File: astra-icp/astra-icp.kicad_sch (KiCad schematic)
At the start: 45 parts, among them J1 Conn_02x05_Top_Bottom

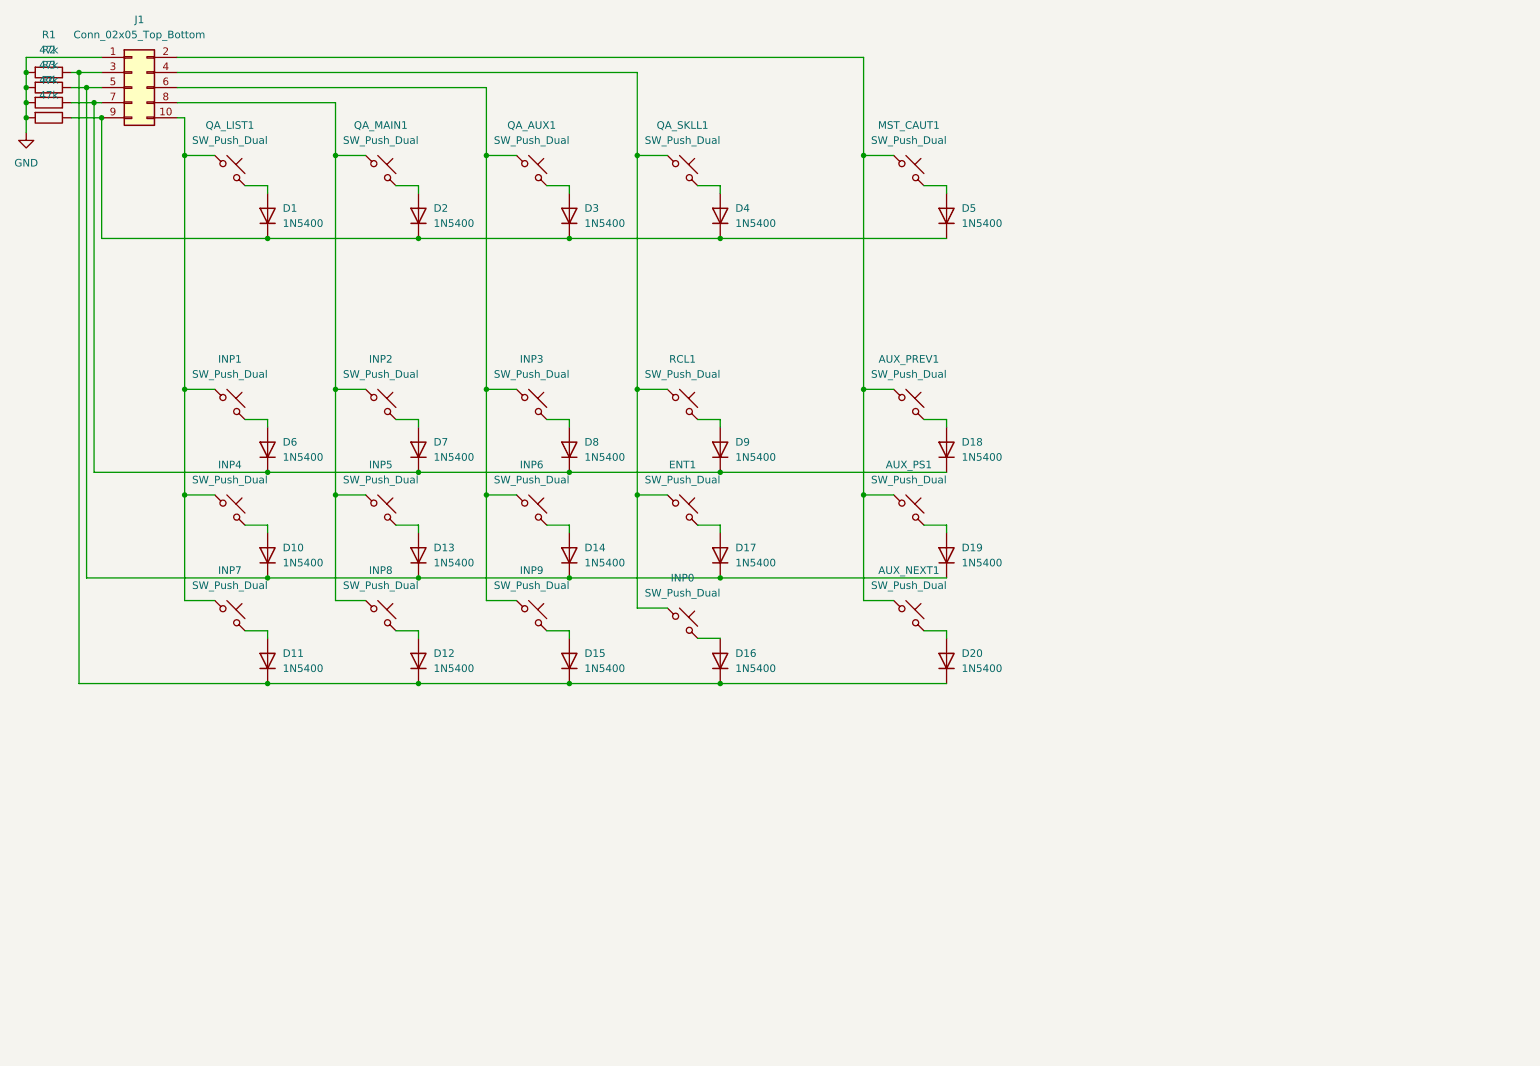
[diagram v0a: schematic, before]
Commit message: feat: Schematic and partial PCB for ICP rev2
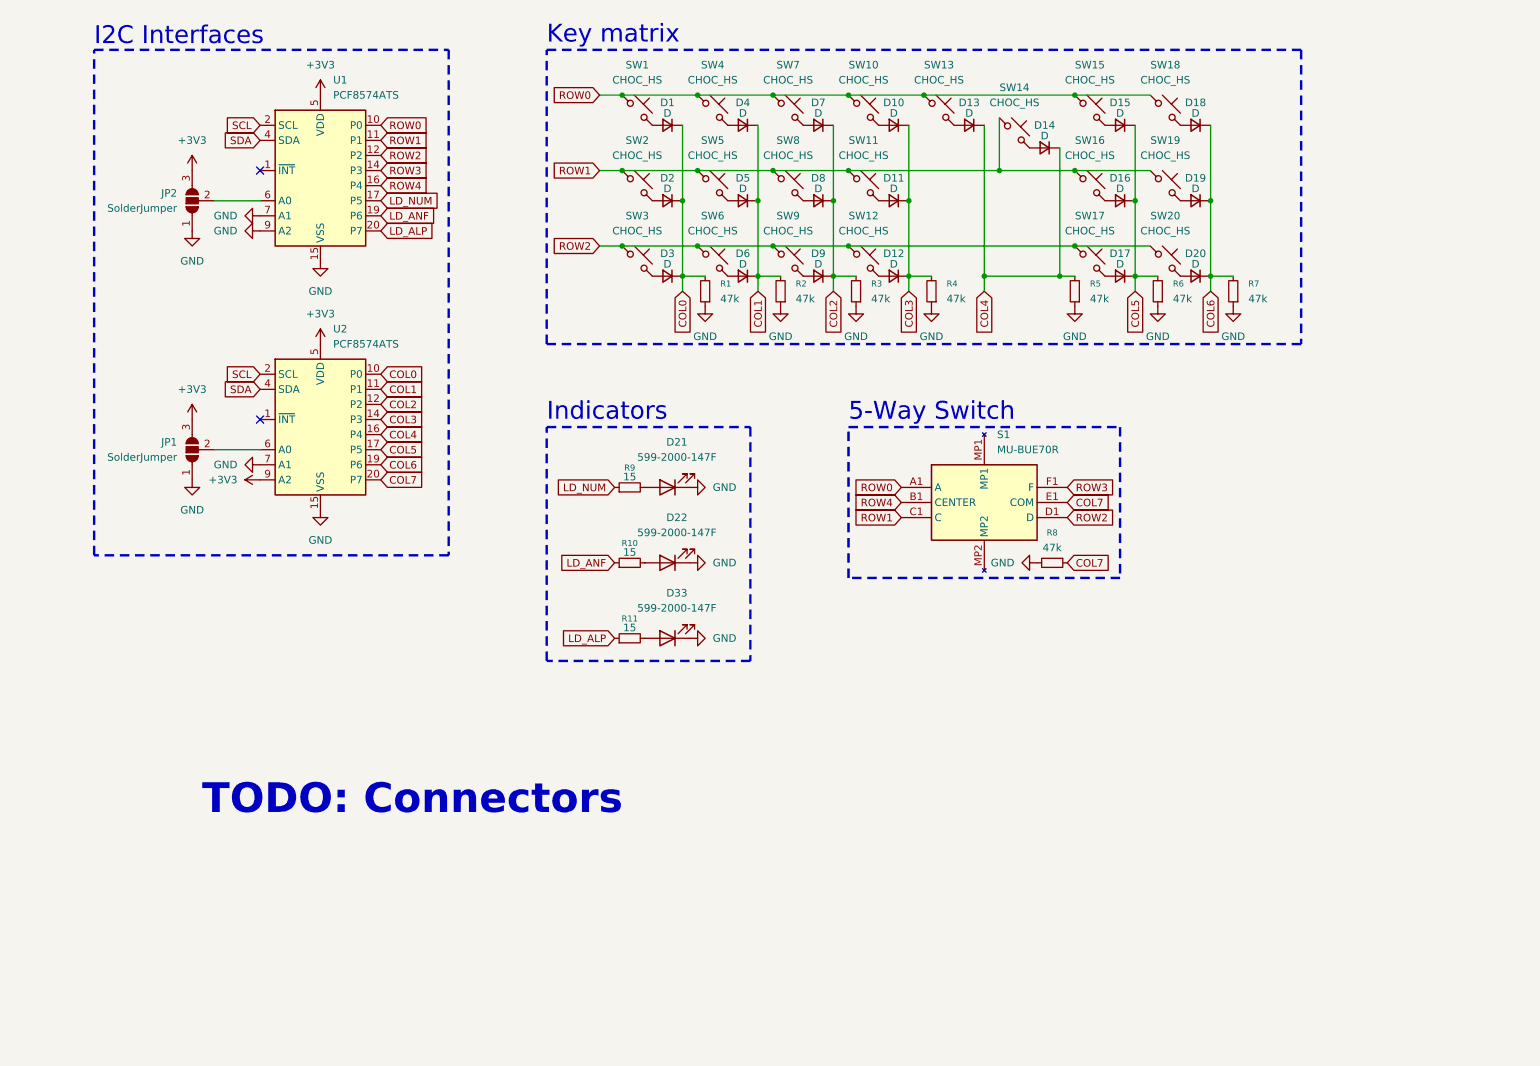
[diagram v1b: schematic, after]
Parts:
- removed AUX_NEXT1, AUX_PREV1, AUX_PS1, ENT1, INP0, INP1, INP2, INP3, INP4, INP5, INP6, INP7, INP8, INP9, MST_CAUT1, QA_AUX1, QA_LIST1, QA_MAIN1, QA_SKLL1, RCL1: SW_Push_Dual, PCM_Switch_Keyboard_Hotswap_Kailh:SW_Hotswap_Kailh_Choc_V2_1.00u, symbol Switch:SW_Push_45deg
- removed D1, D10, D11, D12, D13, D14, D15, D16, D17, D18, D19, D2, D20, D3, D4, D5, D6, D7, D8, D9: 1N5400, Diode_THT:D_DO-41_SOD81_P7.62mm_Horizontal, symbol Diode:1N5400
- removed J1: Conn_02x05_Top_Bottom, Connector_PinSocket_2.00mm:PinSocket_2x05_P2.00mm_Vertical, symbol Connector_Generic:Conn_02x05_Odd_Even
- removed R1, R2, R3, R4: 47k, Resistor_SMD:R_2512_6332Metric_Pad1.40x3.35mm_HandSolder, symbol PCM_SL_Resistors:47k
- added D1, D10, D11, D12, D13, D14, D15, D16, D17, D18, D19, D2, D20, D3, D4, D5, D6, D7, D8, D9: D, PCM_Diode_SMD_AKL:D_0603_1608Metric_Pad1.05x0.95mm_HandSolder, symbol Device:D_Small
- added D21, D22, D33: 599-2000-147F, LED_SMD:LED_0603_1608Metric_Pad1.05x0.95mm_HandSolder, symbol Device:LED
- added JP1, JP2: SolderJumper, Jumper:SolderJumper-3_P2.0mm_Open_TrianglePad1.0x1.5mm, symbol Jumper:SolderJumper_3_Open
- added R1, R2, R3, R4, R5, R6, R7, R8: 47k, PCM_Resistor_SMD_AKL:R_0201_0603Metric_Pad0.64x0.40mm_HandSolder, symbol Device:R_Small
- added R10, R11, R9: 15, PCM_Resistor_SMD_AKL:R_0201_0603Metric_Pad0.64x0.40mm_HandSolder, symbol Device:R_Small
- added S1: MU-BUE70R, footprints:MUBUE70R, symbol MU-BUE70R:MU-BUE70R
- added SW1, SW10, SW11, SW12, SW13, SW14, SW15, SW16, SW17, SW18, SW19, SW2, SW20, SW3, SW4, SW5, SW6, SW7, SW8, SW9: CHOC_HS, PCM_Switch_Keyboard_Hotswap_Kailh:SW_Hotswap_Kailh_Choc_V1V2_1.00u, symbol Switch:SW_Push_45deg
- added U1, U2: PCF8574ATS, Package_SO:SSOP-20_4.4x6.5mm_P0.65mm, symbol Interface_Expansion:PCF8574ATS
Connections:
- net GND: now also D21.1 (K), D22.1 (K), D33.1 (K), JP1.1 (A), JP2.1 (A), R1.1, R2.1, R3.1, R4.1, R5.1, R6.1, R7.1, R8.2, U1.15 (VSS), U1.7 (A1), U1.9 (A2), U2.15 (VSS), U2.7 (A1)
- new net: D6.2 (A), SW6.2
- new net: D13.2 (A), SW13.2
- new net: D22.2 (A), R10.2
- new net: D14.2 (A), SW14.2
- new net: D16.2 (A), SW16.2
- new net: D8.2 (A), SW8.2
- new net: JP1.2 (C), U2.6 (A0)
- new net: D2.2 (A), SW2.2
- new net: D17.2 (A), SW17.2
- new net: D11.2 (A), SW11.2
- new net: D33.2 (A), R11.2
- new net: D7.2 (A), SW7.2
- new net: D18.2 (A), SW18.2
- new net: D5.2 (A), SW5.2
- new net: D12.2 (A), SW12.2
- new net: D19.2 (A), SW19.2
- new net: D21.2 (A), R9.2
- new net: D3.2 (A), SW3.2
- new net: D20.2 (A), SW20.2
- new net: D4.2 (A), SW4.2
- new net: D9.2 (A), SW9.2
- new net: JP2.2 (C), U1.6 (A0)
- new net: D10.2 (A), SW10.2
- new net: D15.2 (A), SW15.2
- new net: D1.2 (A), SW1.2
- new net +3V3: JP1.3 (B), JP2.3 (B), U1.5 (VDD), U2.5 (VDD), U2.9 (A2)
- new net COL0: D1.1 (K), D2.1 (K), D3.1 (K), R1.2, U2.10 (P0)
- new net COL1: D4.1 (K), D5.1 (K), D6.1 (K), R2.2, U2.11 (P1)
- new net COL2: D7.1 (K), D8.1 (K), D9.1 (K), R3.2, U2.12 (P2)
- new net COL3: D10.1 (K), D11.1 (K), D12.1 (K), R4.2, U2.14 (P3)
- new net COL4: D13.1 (K), D14.1 (K), R5.2, U2.16 (P4)
- new net COL5: D15.1 (K), D16.1 (K), D17.1 (K), R6.2, U2.17 (P5)
- new net COL6: D18.1 (K), D19.1 (K), D20.1 (K), R7.2, U2.19 (P6)
- new net COL7: R8.1, S1.E1 (COM), U2.20 (P7)
- new net LD_ALP: R11.1, U1.20 (P7)
- new net LD_ANF: R10.1, U1.19 (P6)
- new net LD_NUM: R9.1, U1.17 (P5)
- new net ROW0: S1.A1 (A), SW1.1, SW10.1, SW13.1, SW15.1, SW18.1, SW4.1, SW7.1, U1.10 (P0)
- new net ROW1: S1.C1 (C), SW11.1, SW14.1, SW16.1, SW19.1, SW2.1, SW5.1, SW8.1, U1.11 (P1)
- new net ROW2: S1.D1 (D), SW12.1, SW17.1, SW20.1, SW3.1, SW6.1, SW9.1, U1.12 (P2)
- new net ROW3: S1.F1 (F), U1.14 (P3)
- new net ROW4: S1.B1 (CENTER), U1.16 (P4)
- new net SCL: U1.2 (SCL), U2.2 (SCL)
- new net SDA: U1.4 (SDA), U2.4 (SDA)
- no-connect marks 0 -> 2
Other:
- note added: "5-Way Switch"
- note added: "I2C Interfaces"
- note added: "Indicators"
- note added: "Key matrix"
- note added: "TODO: Connectors"
- title: (none) -> AstraOS-ICP

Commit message: feat: Added MCU and CAN controller+transmitter
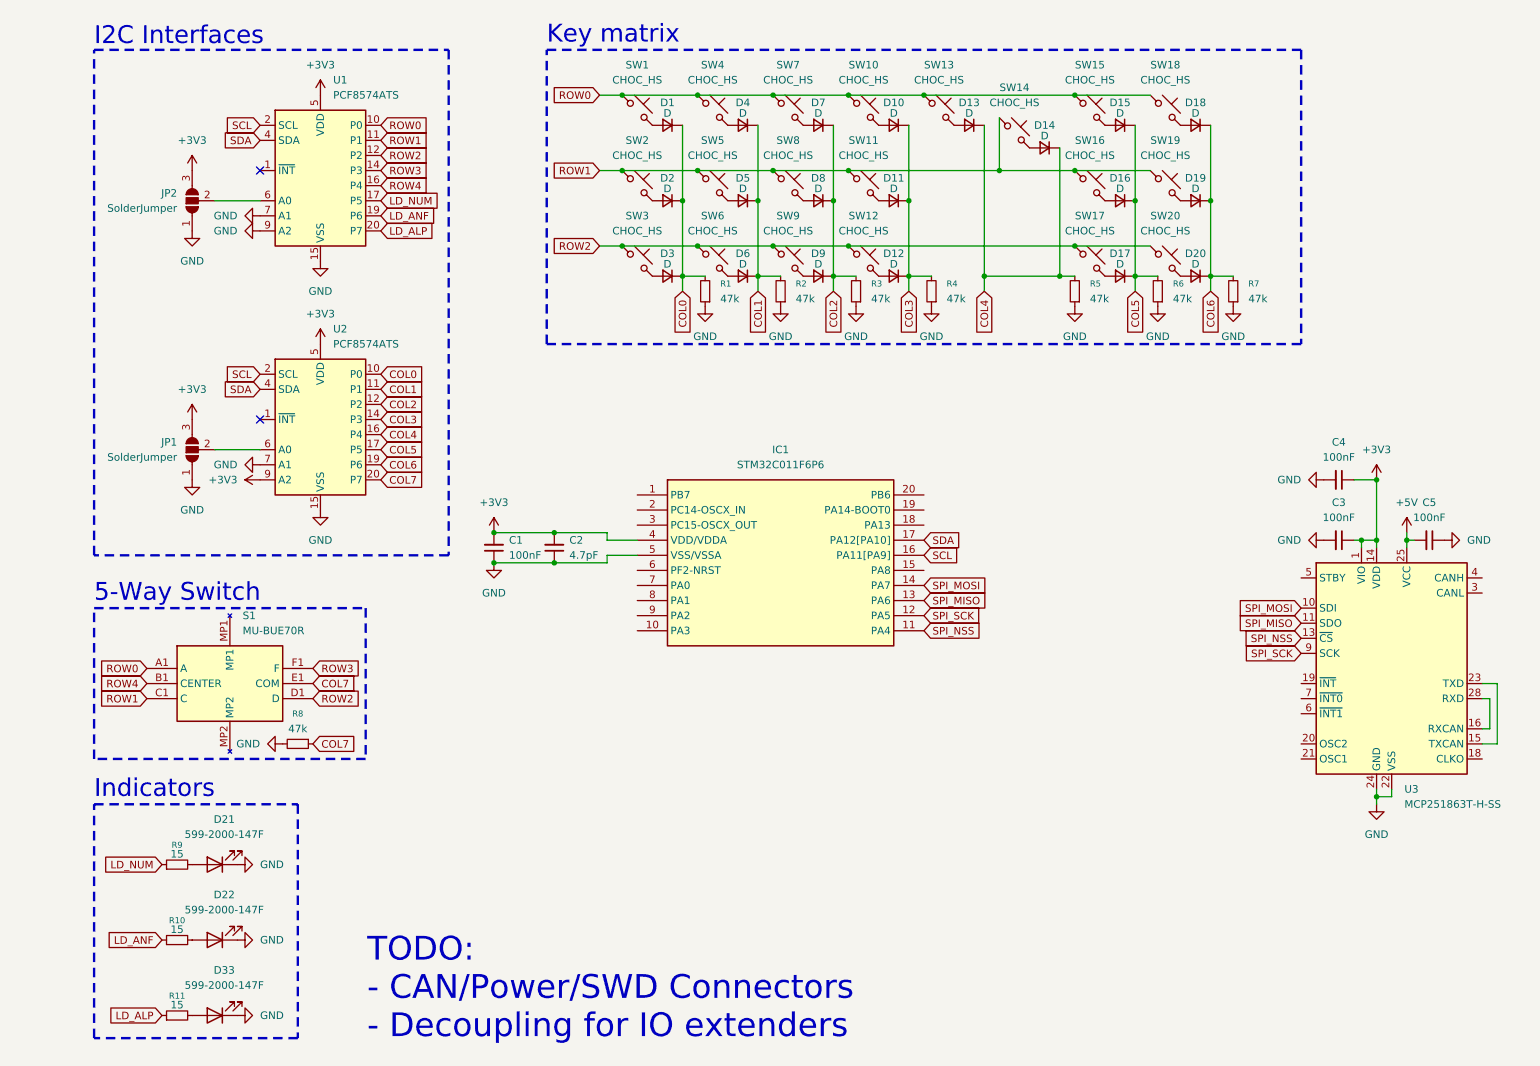
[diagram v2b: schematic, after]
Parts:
- added C1, C3, C4, C5: 100nF, Capacitor_SMD:C_0805_2012Metric, symbol Device:C_Small
- added C2: 4.7pF, Capacitor_SMD:C_0805_2012Metric, symbol Device:C_Small
- added IC1: STM32C011F6P6, footprints:SOP65P640X120-20N, symbol STM32C011F6P6:STM32C011F6P6
- added U3: MCP251863T-H-SS, Package_SO:SSOP-28_5.3x10.2mm_P0.65mm, symbol Interface_CAN_LIN:MCP251863T-H-SS
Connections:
- net +3V3: now also C1.2, C2.2, C3.1, C4.1, IC1.4 (VDD/VDDA), U3.1 (VIO), U3.14 (VDD)
- net GND: now also C1.1, C2.1, C3.2, C4.2, C5.1, IC1.5 (VSS/VSSA), U3.22 (VSS), U3.24 (GND)
- net SCL: now also IC1.16 (PA11[PA9])
- net SDA: now also IC1.17 (PA12[PA10])
- new net: U3.15 (TXCAN), U3.23 (TXD)
- new net: U3.16 (RXCAN), U3.28 (RXD)
- new net +5V: C5.2, U3.25 (VCC)
- new net SPI_MISO: IC1.13 (PA6), U3.11 (SDO)
- new net SPI_MOSI: IC1.14 (PA7), U3.10 (SDI)
- new net SPI_NSS: IC1.11 (PA4), U3.13 (~{CS})
- new net SPI_SCK: IC1.12 (PA5), U3.9 (SCK)
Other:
- note added: "TODO: - CAN/Power/SWD Connectors - Decoupling for IO extenders"
- note removed: "TODO: Connectors"
- moved on the sheet: D21, D22, D33, R10, R11, R8, R9, S1

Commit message: feat: Work on connectors and MCU-CAN signaling
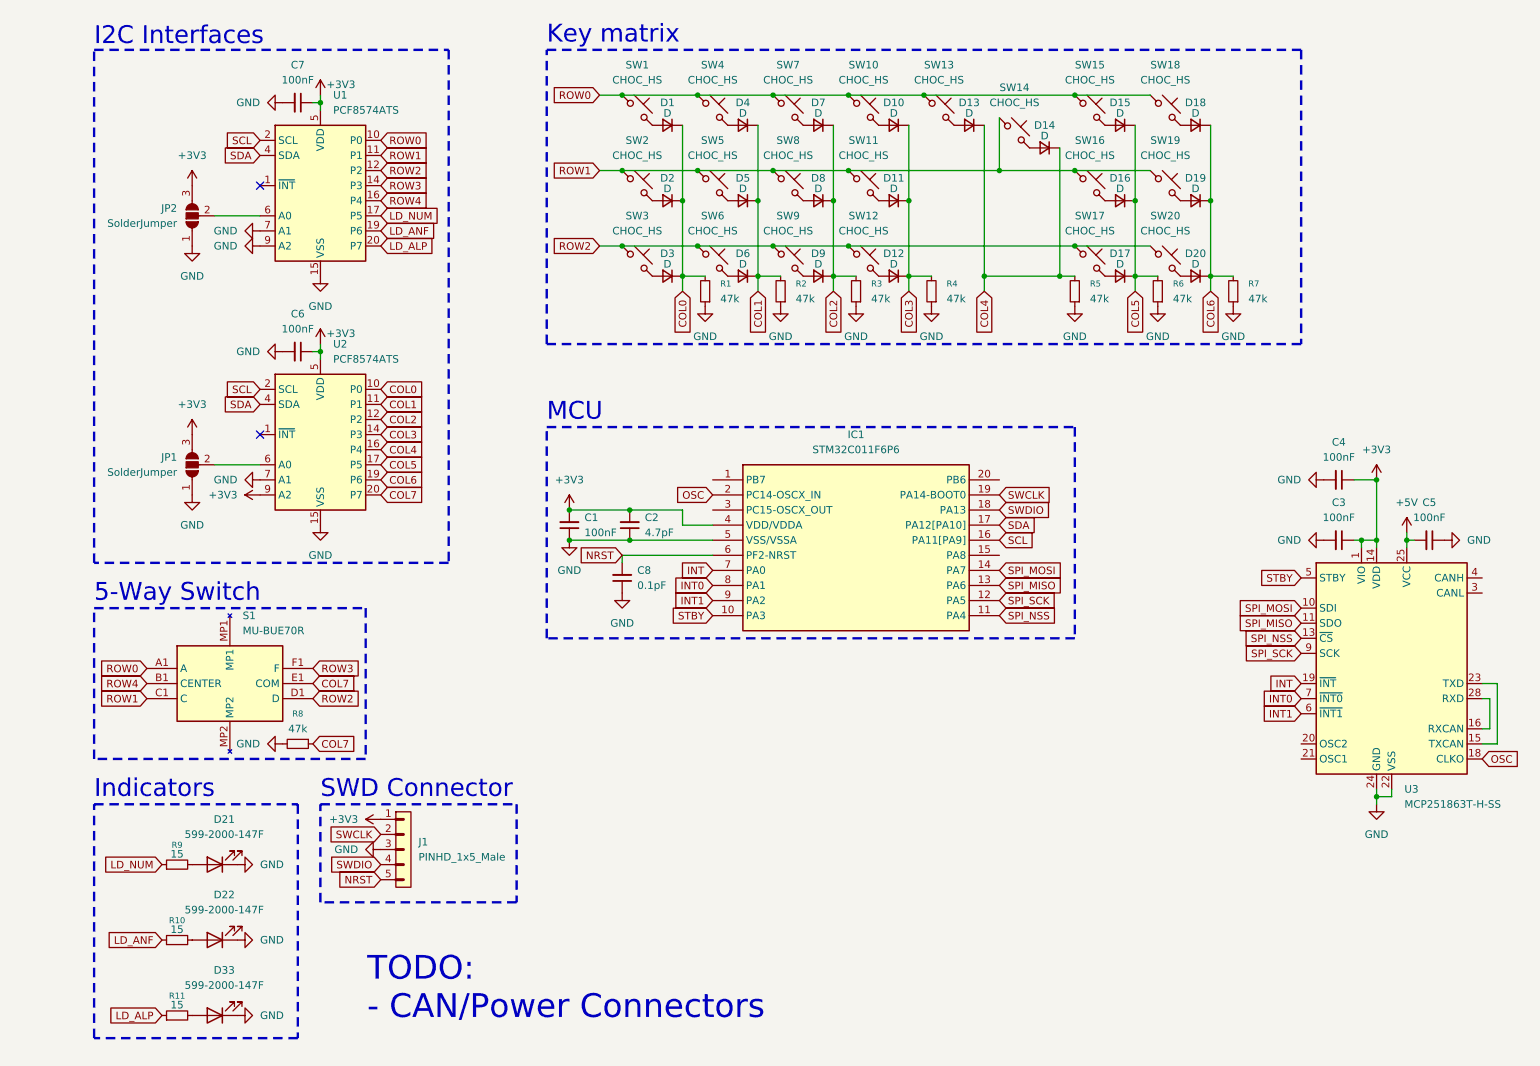
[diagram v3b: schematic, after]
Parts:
- added C6, C7: 100nF, Capacitor_SMD:C_0805_2012Metric, symbol Device:C_Small
- added C8: 0.1pF, Capacitor_SMD:C_0805_2012Metric, symbol Device:C_Small
- added J1: PINHD_1x5_Male, Connector_PinHeader_2.54mm:PinHeader_1x05_P2.54mm_Vertical, symbol PCM_SL_Pin_Headers:PINHD_1x5_Male
- IC1: Height 1.2 -> (none); Manufacturer_Name STMicroelectronics -> (none); Manufacturer_Part_Number STM32C011F6P6 -> (none); Mouser Part Number 511-STM32C011F6P6 -> (none); Mouser Price/Stock https://www.mouser.co.uk/ProductDetail/STMicroelectronics/S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 -> (none); Part Number (none) -> STM32C011F6P6
- S1: Height 7.2 -> (none); Manufacturer_Name Apem -> (none); Manufacturer_Part_Number MU-BUE70R -> (none); Part Number (none) -> MU-BUE70R
- U1, U2: Part Number (none) -> PCF8574APWR
- U3: Part Number (none) -> MCP251863T-H/SS
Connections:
- net +3V3: now also C6.1, C7.1, J1.1
- net GND: now also C6.2, C7.2, C8.1, J1.3
- net STBY: now reaches IC1.10 (PA3)
- net STBY: now also U3.5 (STBY)
- net SWDIO: now reaches IC1.18 (PA13)
- net SWDIO: now also J1.4
- net SWCLK: now reaches IC1.19 (PA14-BOOT0)
- net SWCLK: now also J1.2
- net OSC: now reaches IC1.2 (PC14-OSCX_IN)
- net OSC: now also U3.18 (CLKO)
- net NRST: now reaches IC1.6 (PF2-NRST)
- net NRST: now also C8.2, J1.5
- net INT: now reaches IC1.7 (PA0)
- net INT: now also U3.19 (~{INT})
- net INT0: now reaches IC1.8 (PA1)
- net INT0: now also U3.7 (~{INT0})
- net INT1: now reaches IC1.9 (PA2)
- net INT1: now also U3.6 (~{INT1})
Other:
- note added: "MCU"
- note added: "SWD Connector"
- note added: "TODO: - CAN/Power Connectors"
- note removed: "TODO: - CAN/Power/SWD Connectors - Decoupling for IO extenders"
- moved on the sheet: C1, C2, IC1, JP1, JP2, U1, U2
